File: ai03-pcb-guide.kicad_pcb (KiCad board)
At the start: 2 copper layers, 78.7 x 38.1 mm, 24 parts, among them SW1 SW_Push, U1 ATmega32U4-AU, Y1 Crystal_GND24_Small

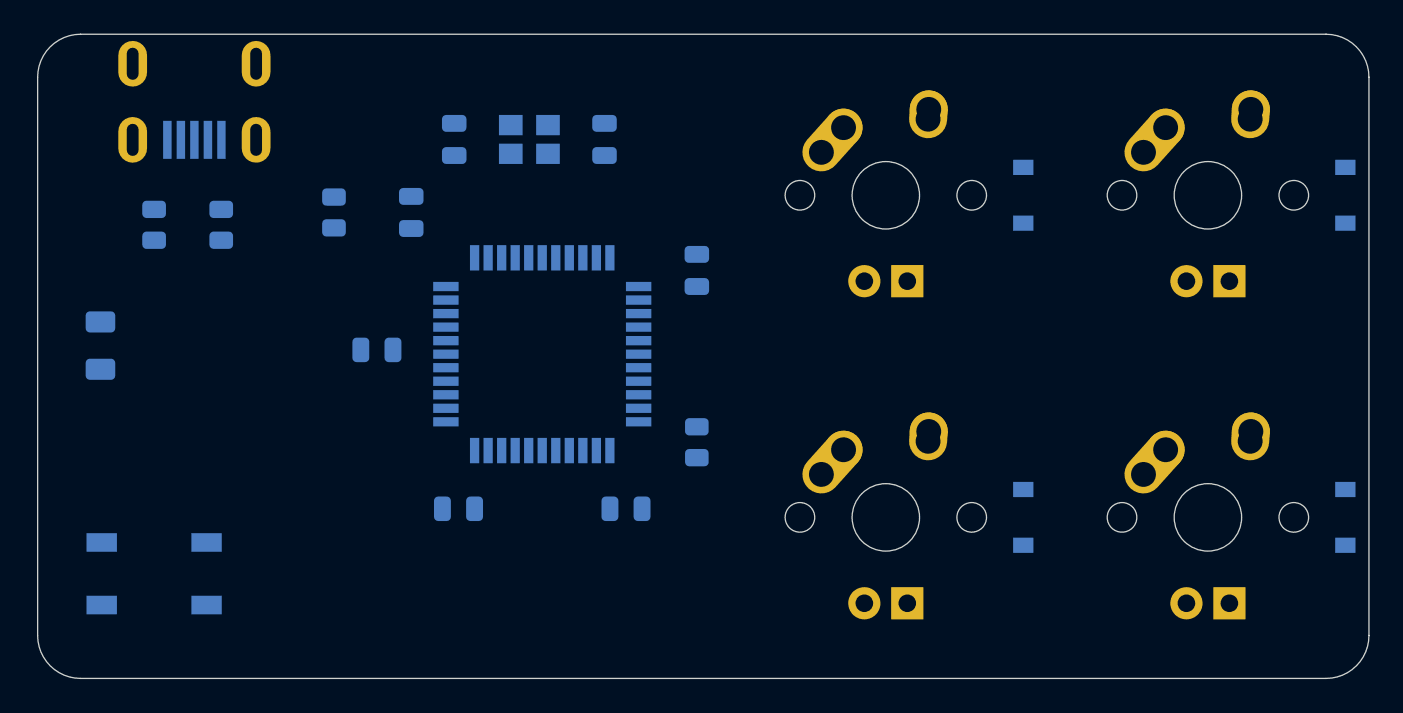
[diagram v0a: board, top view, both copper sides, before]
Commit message: ステップ9、10 配線。
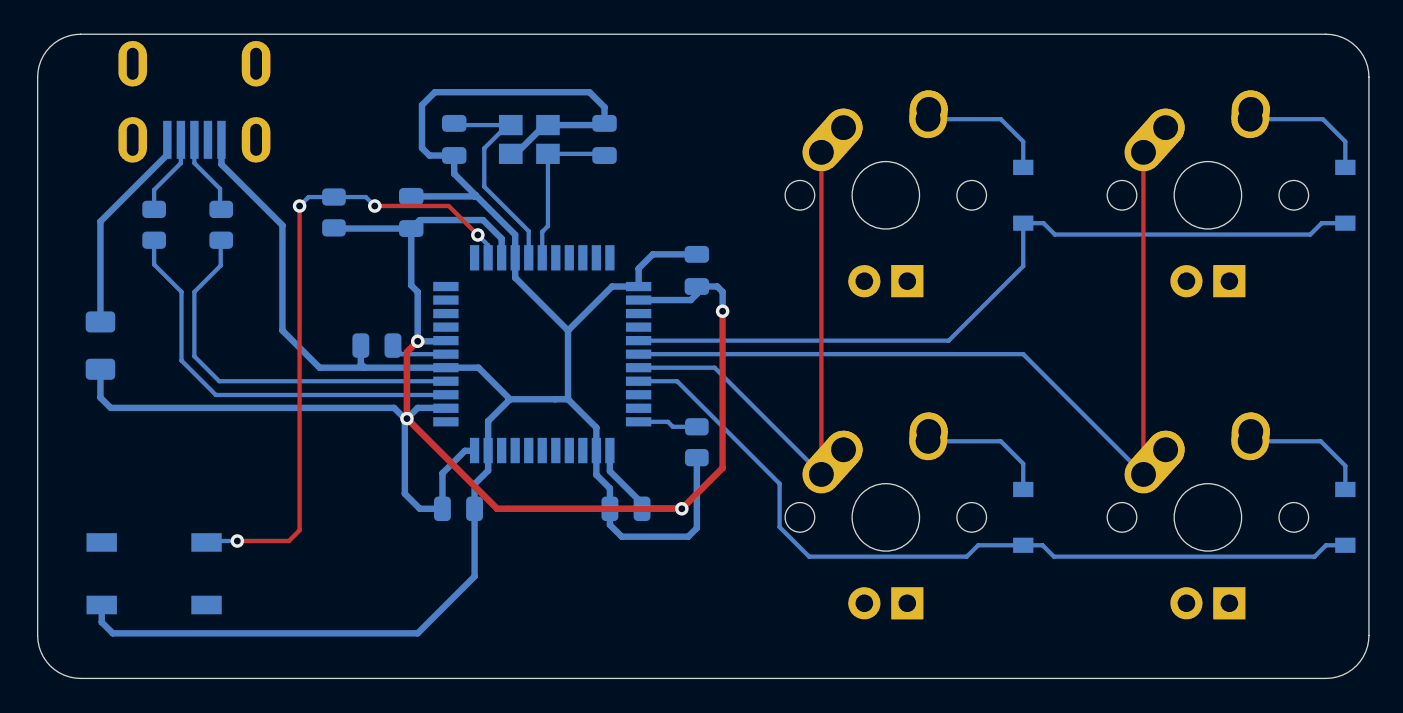
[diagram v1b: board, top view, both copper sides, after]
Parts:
- moved C3 0.25 mm to (65.8, 92.1)
- turned F1 to 90 degrees
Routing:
- net GND: track 0.00 -> 141.7 mm
- net +5V: track 0.00 -> 104.2 mm, vias 0 -> 4
- net COL1: track 0.00 -> 51.9 mm
- net ROW1: track 0.00 -> 48.4 mm
- net ROW0: track 0.00 -> 46.7 mm
- net Net-(R1-Pad2): track 0.00 -> 38.4 mm, vias 0 -> 4
- net COL0: track 0.00 -> 32.5 mm
- net Net-(R3-Pad1): track 0.00 -> 24.3 mm
- net Net-(R2-Pad1): track 0.00 -> 23.1 mm
- net Net-(C2-Pad1): track 0.00 -> 13.1 mm
- net VCC: track 0.00 -> 12.4 mm
- net Net-(C1-Pad1): track 0.00 -> 9.68 mm
- net Net-(D3-Pad2): track 0.00 -> 7.70 mm
- net Net-(D2-Pad2): track 0.00 -> 7.70 mm
- net Net-(D1-Pad2): track 0.00 -> 7.70 mm
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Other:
- net class Default: trace_width 0.25 -> 0.254
- net class Power added: clearance 0.2, trace_width 0.381, via_dia 0.8, via_drill 0.4

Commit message: ステップ11、ゾーンの塗りつぶし。
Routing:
- added copper zone on B.Cu, net GND

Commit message: ステップ12、デコレーション。
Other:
- board text added: "Hello World!"
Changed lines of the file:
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@@
   (general
     (thickness 1.6)
-    (drawings 8)
+    (drawings 9)
     (tracks 204)
     (zones 0)
@@
     (33 F.Adhes user)
     (34 B.Paste user)
-    (35 F.Paste user)
+    (35 F.Paste user hide)
     (36 B.SilkS user)
     (37 F.SilkS user)
@@
     )
   )
+  (gr_text "Hello World!" (at 51.59375 109.5375) (layer F.SilkS)
+    (effects (font (size 1 1) (thickness 0.15)))
+  )
   (gr_line (start 121.92 73.66) (end 48.26 73.66) (layer Edge.Cuts) (width 0.05))
